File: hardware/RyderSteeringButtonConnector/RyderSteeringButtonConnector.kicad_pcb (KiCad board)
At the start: 2 copper layers, 7 parts, among them J1 Conn_01x04_Pin, J2 Conn_01x05_Pin, J3 Conn_01x03_Pin, J4 Conn_01x03_Pin, J5 Conn_01x03_Pin

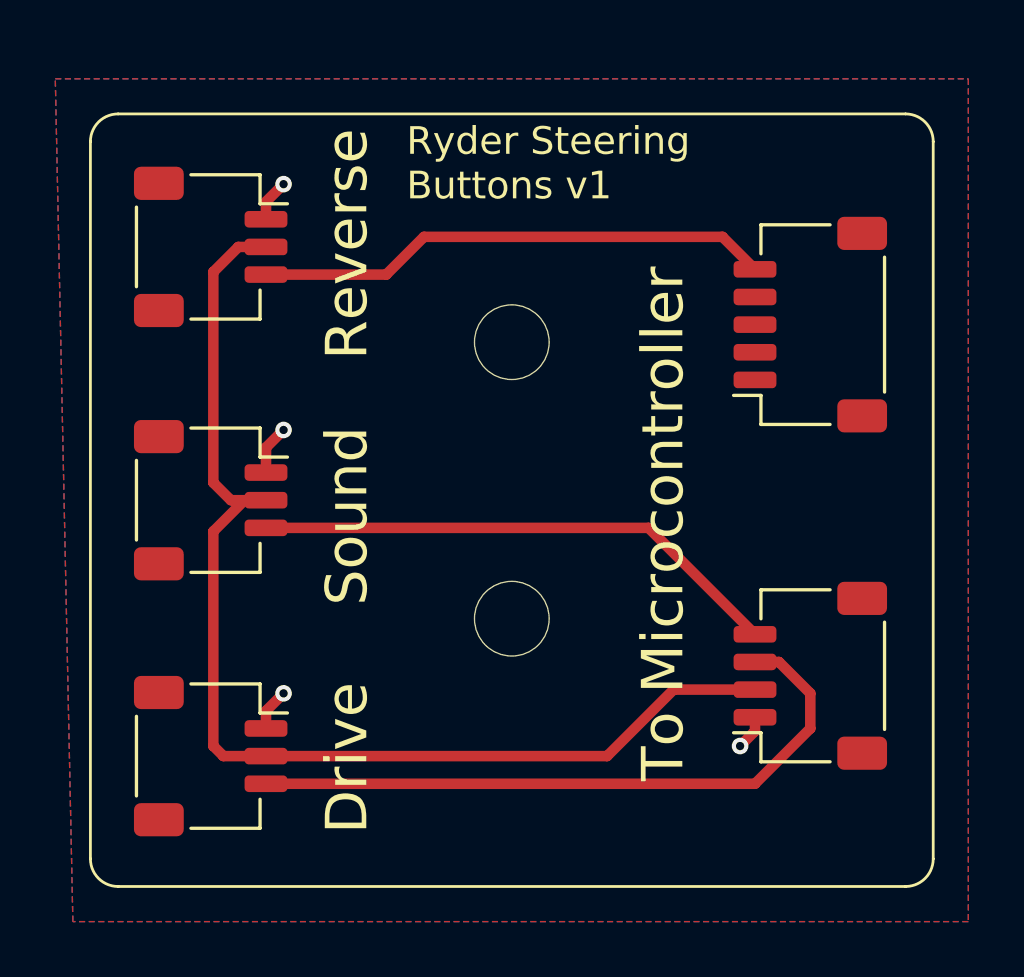
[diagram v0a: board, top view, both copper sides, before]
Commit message: v2 of ryder steering wheel button connnector pcb
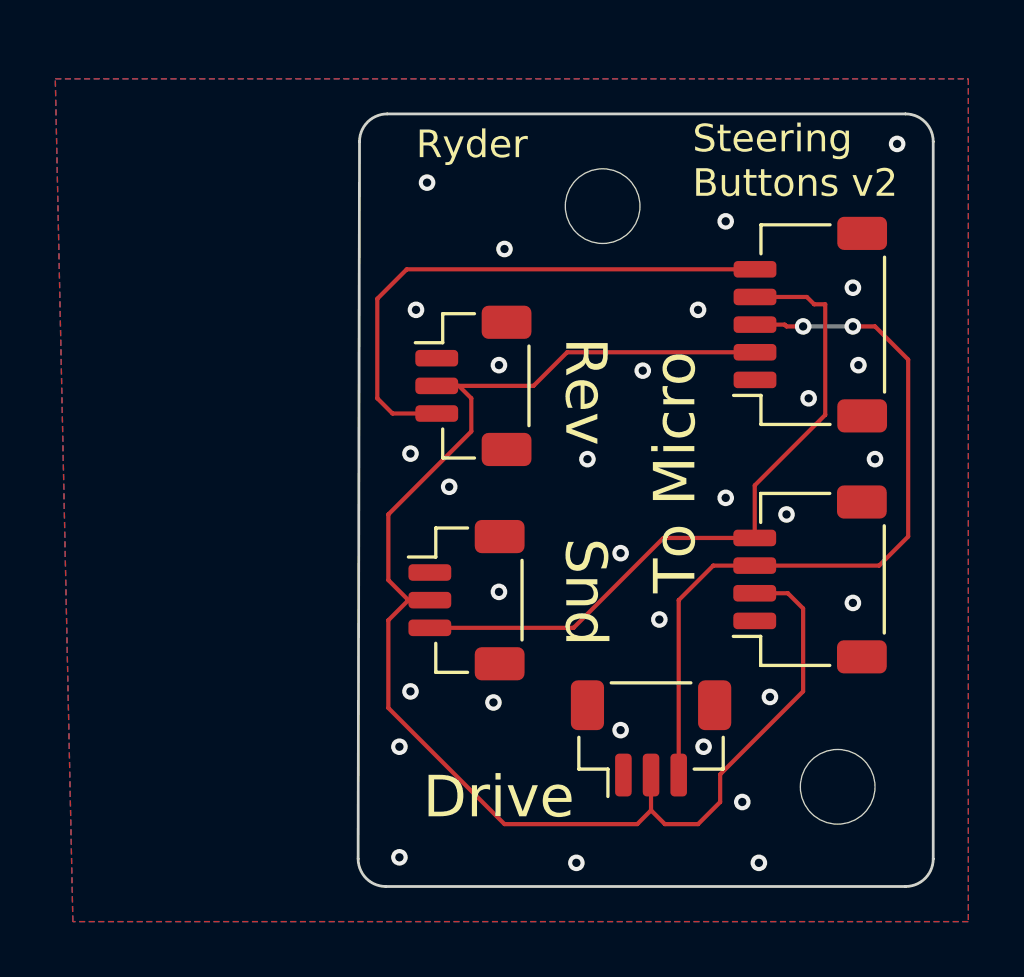
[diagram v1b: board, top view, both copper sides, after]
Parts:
- J3, J4, J5: footprint Connector_JST:JST_SH_SM03B-SRSS-TB_1x03-1MP_P1.00mm_Horizontal -> Connector_JST:JST_SH_BM03B-SRSS-TB_1x03-1MP_P1.00mm_Vertical
- moved J3 15.9 mm to (169.5, 104.5), turned to 0 degrees
- moved H2 13.3 mm to (176.2, 106.2)
- moved J5 10.7 mm to (163.1, 91.8)
- moved J4 9.93 mm to (162.8, 99.5)
- moved H1 5.92 mm to (167.8, 85.2)
- moved J1 3.49 mm to (175.2, 98.8)
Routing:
- net +3V3: track 42.9 -> 53.2 mm
- net GND: track 6.13 -> 0.00 mm, vias 4 -> 29
- net SoundButton: track 19.3 -> 25.3 mm
- net DriveButton: track 24.3 -> 28.0 mm, vias 0 -> 2
- net ReverseSwitch: track 18.7 -> 20.1 mm
- net (no net): vias 0 -> 2
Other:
- board outline added: 20.8 x 27.9 mm
- board text added: "Rev"
- board text added: "Ryder"
- board text added: "Ryder Steering Buttons v2"
- board text added: "Snd"
- board text added: "Steering Buttons v2"
- board text added: "To Micro"
- board text removed: "Reverse"
- board text removed: "Ryder Steering Buttons v1"
- board text removed: "Sound"
- board text removed: "To Microcontroller"

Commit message: reworking layout of ryder steering button PCB again
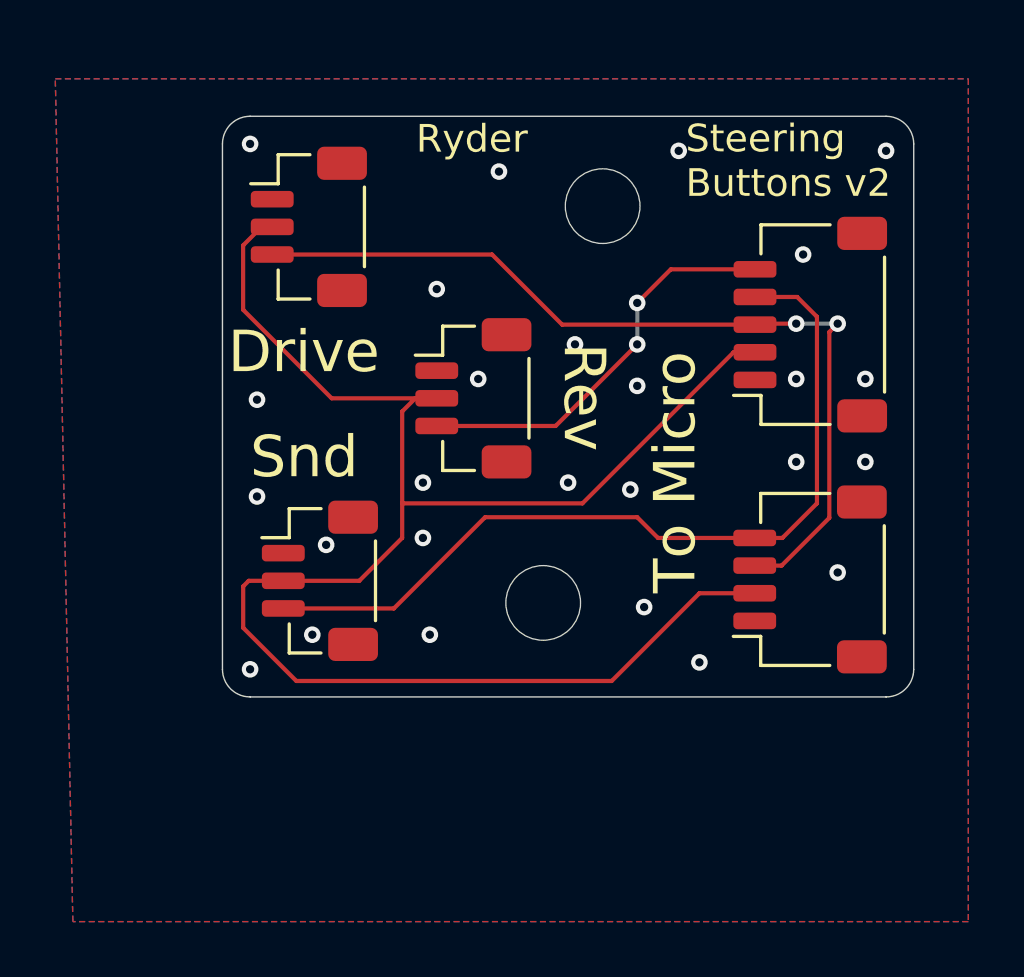
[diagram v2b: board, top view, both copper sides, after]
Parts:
- moved J3 22.3 mm to (157.1, 86.0), turned to -90 degrees
- moved H2 12.6 mm to (165.6, 99.6)
- moved J4 5.35 mm to (157.5, 98.8)
- moved J5 0.45 mm to (163.1, 92.2)
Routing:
- net +3V3: track 53.2 -> 61.6 mm
- net SoundButton: track 25.3 -> 30.8 mm
- net ReverseSwitch: track 20.1 -> 14.7 mm, vias 0 -> 2
- net DriveButton: track 28.0 -> 32.1 mm
- net GND: vias 29 -> 16
- net (no net): vias 2 -> 10
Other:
- board size 20.8 x 27.9 mm -> 25 x 21 mm
